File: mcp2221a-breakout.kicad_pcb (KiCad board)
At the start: 2 copper layers, 22.9 x 27.9 mm, 25 parts, among them J1 USB_B_Micro, J2 LEFT, J3 RIGHT, U1 MCP1700-3302E, U2 MCP2221AxSL

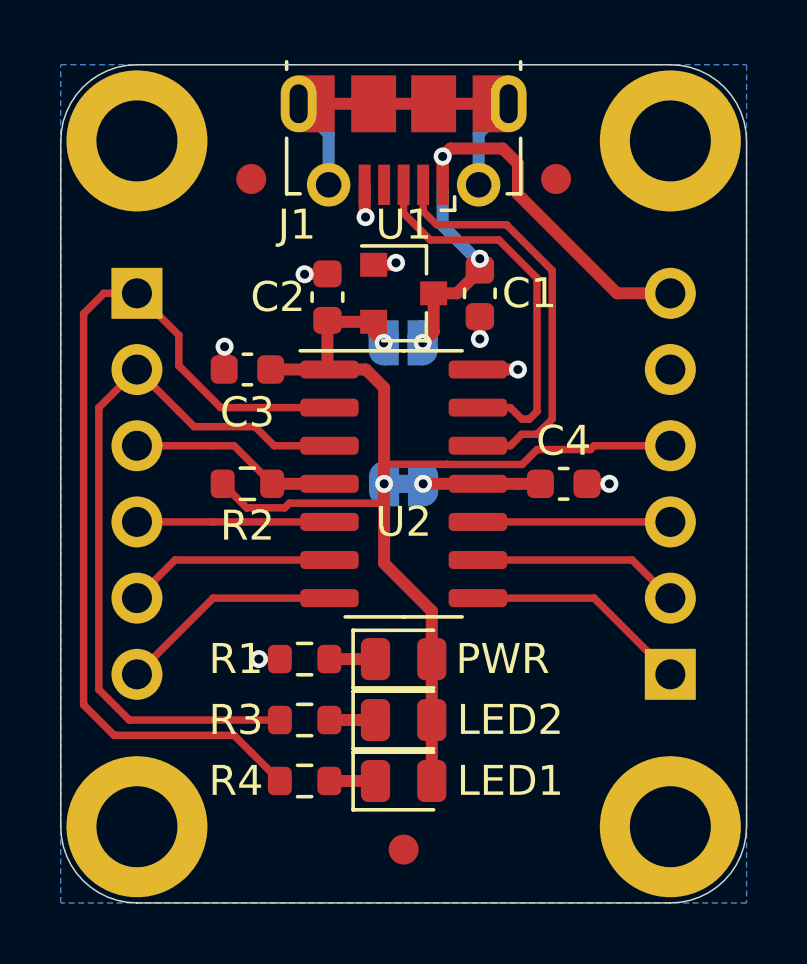
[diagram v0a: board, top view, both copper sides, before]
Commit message: Various Tweaks
* Tidied up the schematic
* Added I2C pullup resistors
* Changed labels on LED1 & LED2 to Rx & Tx
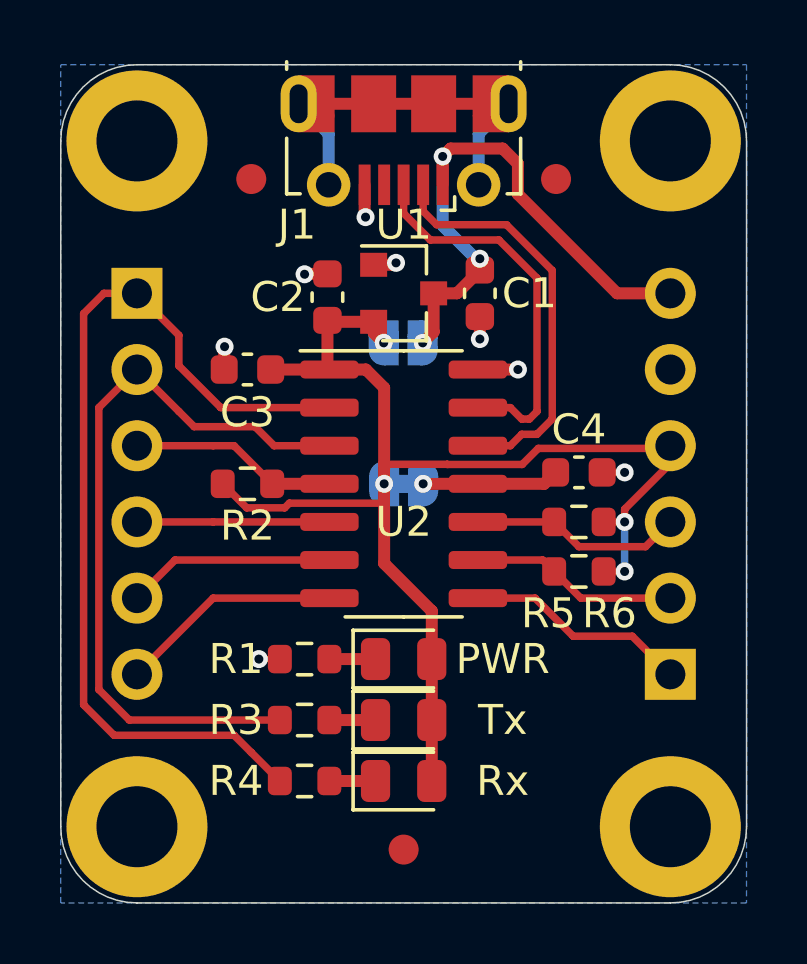
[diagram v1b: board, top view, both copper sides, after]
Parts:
- added R5: 4k7, Resistor_SMD:R_0603_1608Metric, F.Cu at (113.8, 60.1)
- added R6: 4k7, Resistor_SMD:R_0603_1608Metric, F.Cu at (113.8, 58.4)
- D2: value LED2 -> Tx
- D3: value LED1 -> Rx
- moved C4 0.63 mm to (113.8, 56.8)
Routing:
- net VDD: track 38.1 -> 44.3 mm, vias 2 -> 4
- net /SCL: track 6.58 -> 7.26 mm
- net Net-(C4-Pad1): track 3.91 -> 4.57 mm

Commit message: Shrink board outline more
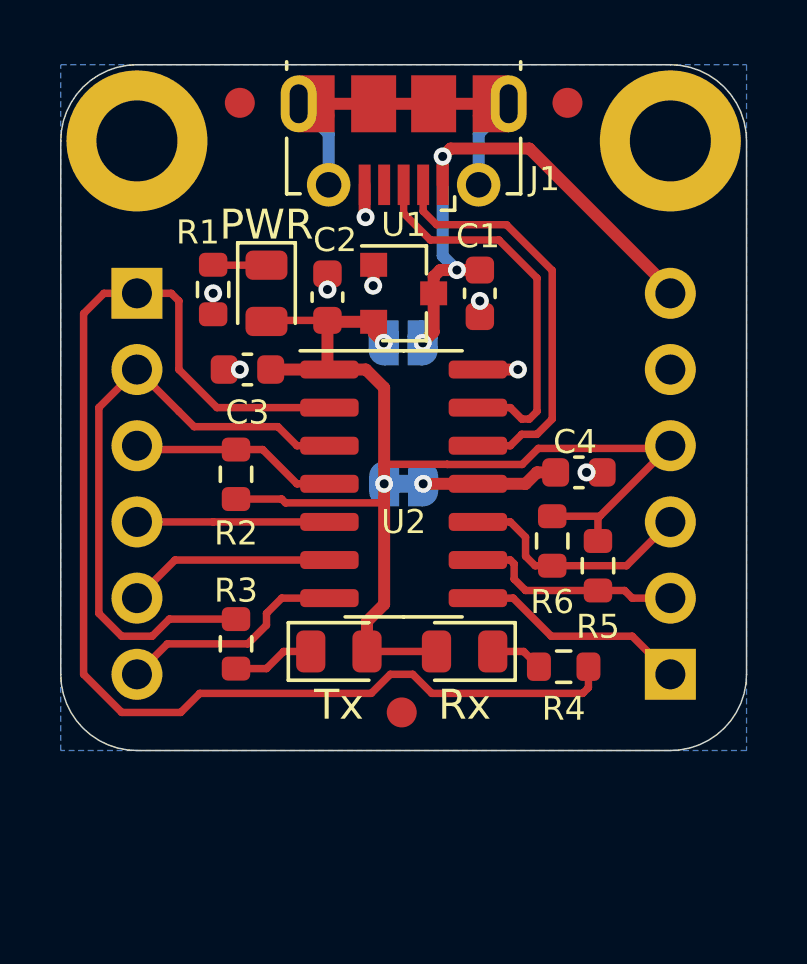
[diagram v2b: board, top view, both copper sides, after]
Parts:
- removed H2, H4: MountingHole, MountingHole:MountingHole_2.7mm_M2.5_DIN965_Pad
- moved D1 13.0 mm to (103.4, 50.8), turned to 270 degrees
- moved R1 12.7 mm to (101.6, 50.7), turned to 90 degrees
- moved R4 9.44 mm to (113.3, 63.2), turned to 180 degrees
- moved D3 4.77 mm to (110.0, 62.7), turned to 180 degrees
- moved FID3 4.57 mm to (107.9, 64.8)
- moved R3 3.42 mm to (102.4, 62.5), turned to 270 degrees
- moved D2 3.14 mm to (105.8, 62.7)
- moved FID1 2.57 mm to (102.5, 44.5)
- moved FID2 2.57 mm to (113.4, 44.5)
- moved R6 1.09 mm to (112.9, 59.1), turned to 90 degrees
- moved R5 0.66 mm to (114.4, 59.9), turned to 90 degrees
- moved R2 0.50 mm to (102.4, 56.8), turned to 270 degrees
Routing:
- net /GP0: track 31.3 -> 42.3 mm
- net /GP1: track 25.1 -> 21.2 mm
- net VDD: track 44.3 -> 42.2 mm, vias 4 -> 2
- net Net-(D2-Pad1): track 1.54 -> 2.73 mm
- net GND: track 6.93 -> 5.91 mm
- net /SCL: track 7.26 -> 8.16 mm
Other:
- board size 22.9 x 27.9 mm -> 22.9 x 22.9 mm
- board text added: "MCP2221A Breakout TB403 20210716"
- board text added: "VBU"
- board text removed: "MCP2221A Breakout Board TB403 21-07-16"
- board text removed: "VBUS"

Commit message: Switch regulator
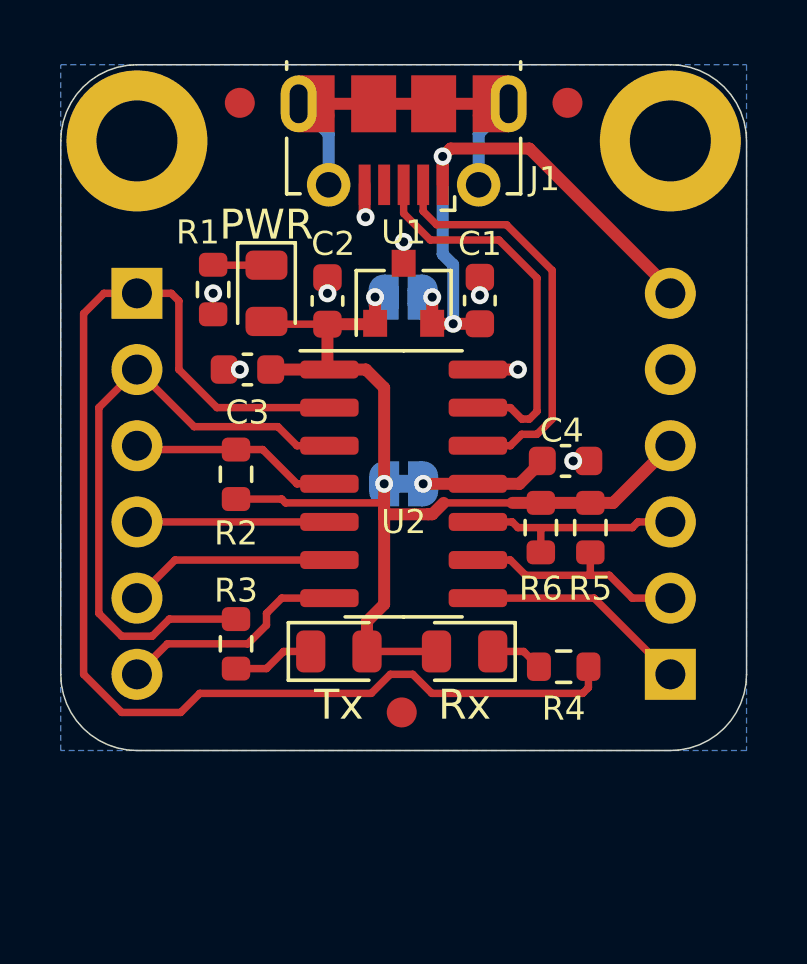
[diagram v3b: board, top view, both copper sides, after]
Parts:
- U1: value MCP1700-3302E -> MCP1812AT-033_TT
- moved JP1 1.52 mm to (107.9, 50.9)
- moved R5 1.30 mm to (114.2, 58.6)
- moved R6 0.59 mm to (112.5, 58.6)
- moved C4 0.59 mm to (113.3, 56.4)
- moved C1 0.24 mm to (110.5, 51.0), turned to 90 degrees
- moved C2 0.13 mm to (105.4, 51.1)
- turned U1 to 90 degrees
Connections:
- U1 pad 1: GND -> VDD
- U1 pad 2: VDD -> VBUS
- U1 pad 3: VBUS -> GND
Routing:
- net VDD: track 42.2 -> 38.6 mm
- net /SCL: track 8.16 -> 7.56 mm
- net VBUS: track 19.5 -> 18.9 mm

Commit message: Update for KICAD 6.0
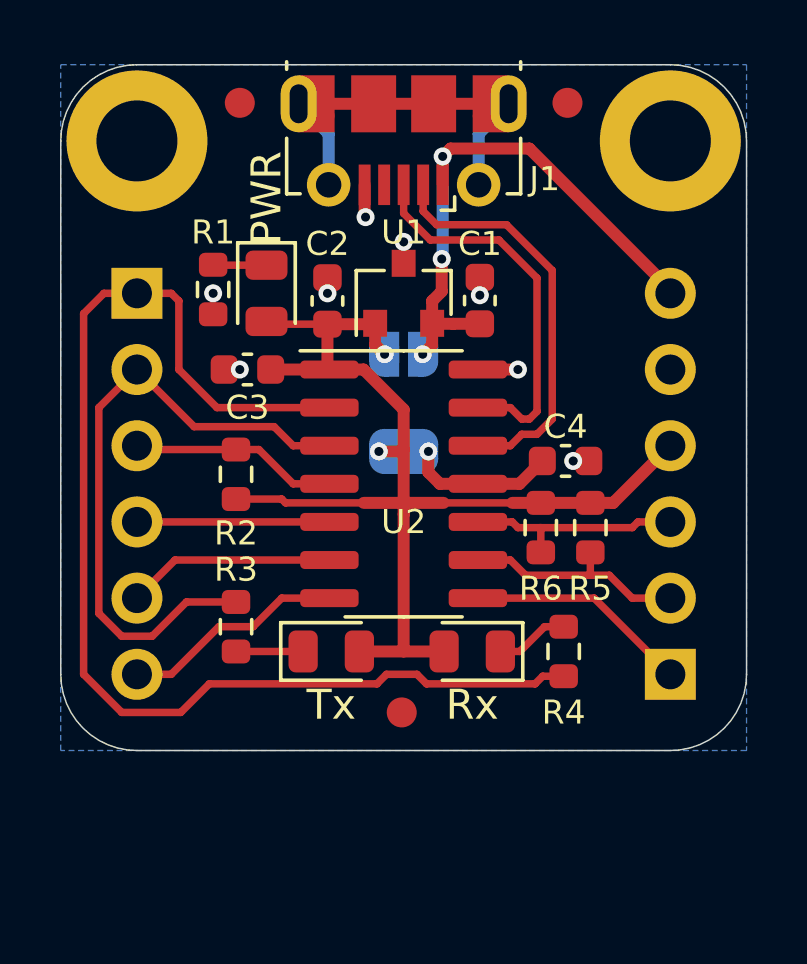
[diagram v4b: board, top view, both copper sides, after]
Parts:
- removed H3: MountingHole, MountingHole:MountingHole_2.7mm_M2.5_DIN965_Pad
- added H2: MountingHole, MountingHole:MountingHole_2.7mm_M2.5_DIN965_Pad, F.Cu at (116.8, 45.7)
- moved JP1 1.91 mm to (108.0, 52.8)
- moved JP2 1.08 mm to (108.0, 56.1)
- moved R3 0.57 mm to (102.4, 61.9)
- moved R4 0.51 mm to (113.3, 62.7), turned to 90 degrees
- moved D3 0.25 mm to (110.2, 62.7)
- moved D2 0.25 mm to (105.5, 62.7)
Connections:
- net /~RST renamed /~{RST}
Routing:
- net /GP0: track 42.3 -> 40.7 mm
- net VDD: track 38.6 -> 40.1 mm
- net Net-(D3-Pad1): track 1.75 -> 2.45 mm
- net Net-(C4-Pad1): track 4.29 -> 4.97 mm
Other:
- net class Default removed
- board text added: "~{RST}"
- board text removed: "~RST"
